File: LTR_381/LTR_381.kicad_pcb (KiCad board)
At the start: 2 copper layers, 25.4 x 17.8 mm, 26 parts, among them J1 Conn_01x06, J2 Conn_01x04, J3 Conn_01x06, J4 Conn_01x04, Q1 BSS138DW, Q2 BSS138DW, U1 AP2127K-3.3

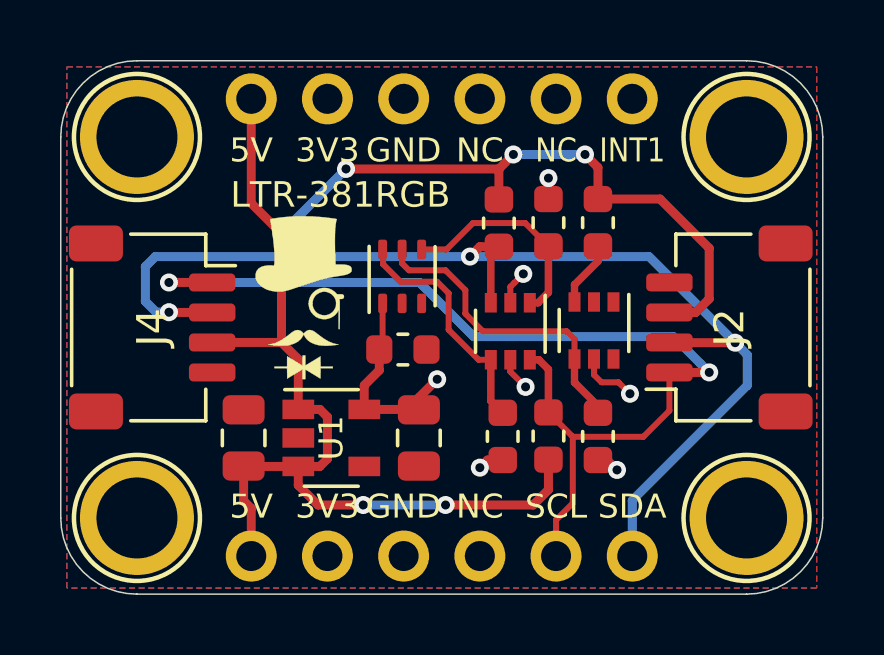
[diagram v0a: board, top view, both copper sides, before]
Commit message: Board Revision
Ground plane joined, SCL, SDA and INT broken out on both sides of headers
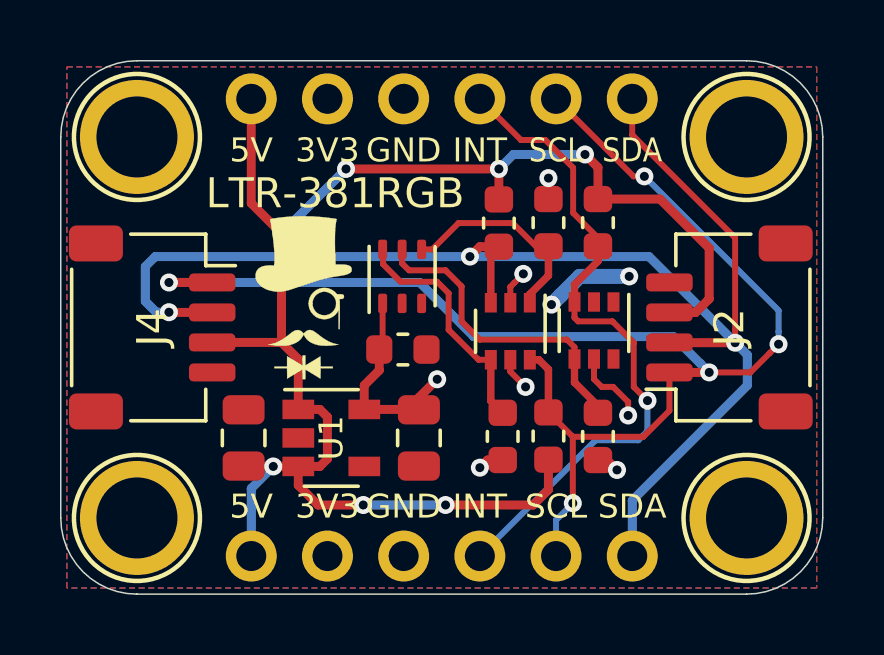
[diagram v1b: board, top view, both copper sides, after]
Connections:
- J1 pad 4: Net-(J1-Pad4) -> INT_5V
- J3 pad 4: Net-(J3-Pad4) -> INT_5V
- J3 pad 5: Net-(J3-Pad5) -> SCL_5V
- J3 pad 6: INT1 -> SDA_5V
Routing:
- net INT_5V: track 2.18 -> 22.5 mm, vias 0 -> 1
- net SCL_5V: track 34.4 -> 48.6 mm, vias 2 -> 5
- net SDA_5V: track 38.7 -> 48.2 mm
- net GND: track 0.00 -> 2.98 mm, vias 0 -> 2
- net 3V3: track 13.5 -> 14.1 mm
- net 5V: track 53.7 -> 53.9 mm, vias 6 -> 7
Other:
- board text added: "INT"
- board text removed: "INT1"
- board text removed: "NC"

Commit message: Auto stash before revert of "Board Revision"
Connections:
- J1 pad 4: INT_5V -> Net-(J1-Pad4)
- J3 pad 4: INT_5V -> Net-(J3-Pad4)
- J3 pad 5: SCL_5V -> Net-(J3-Pad5)
- J3 pad 6: SDA_5V -> INT1
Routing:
- net INT_5V: track 22.5 -> 2.18 mm, vias 1 -> 0
- net SCL_5V: track 48.6 -> 34.4 mm, vias 5 -> 2
- net SDA_5V: track 48.2 -> 38.7 mm
- net GND: track 2.98 -> 0.00 mm, vias 2 -> 0
- net 3V3: track 14.1 -> 13.5 mm
- net 5V: track 53.9 -> 53.7 mm, vias 7 -> 6
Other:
- board text added: "INT1"
- board text added: "NC"
- board text removed: "INT"
